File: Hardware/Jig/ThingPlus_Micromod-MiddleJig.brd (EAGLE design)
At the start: 104.1 x 35.6 mm, 67 parts

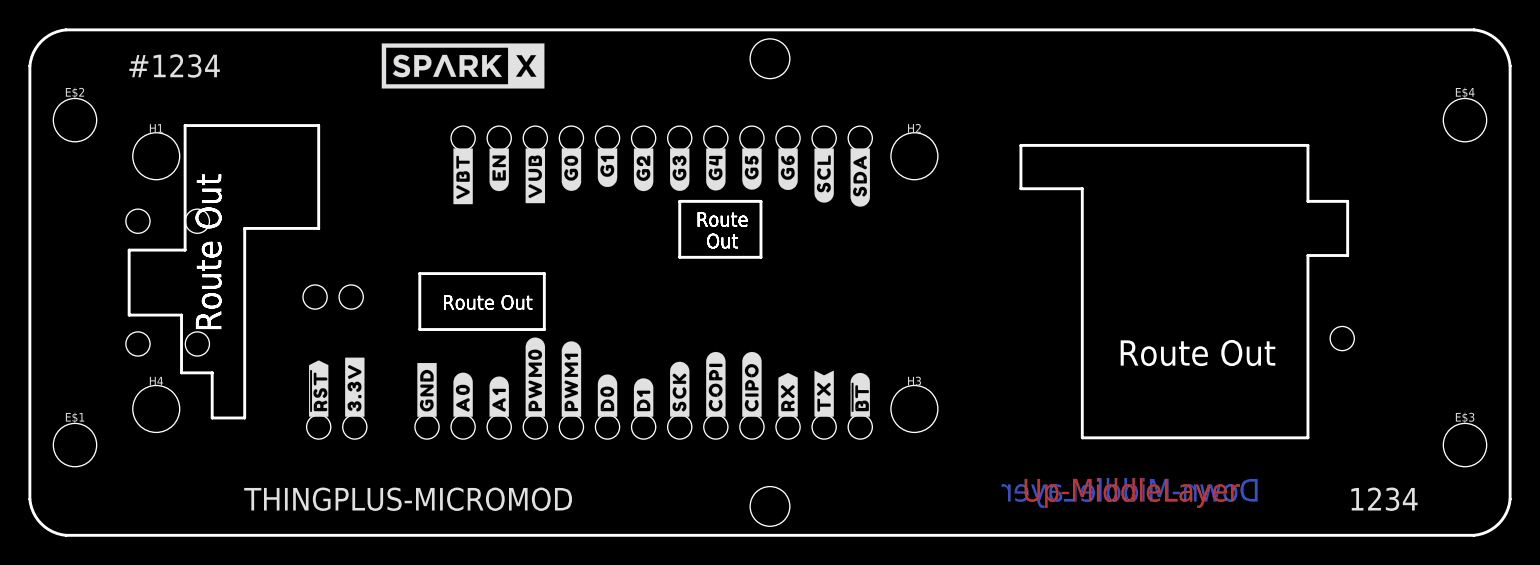
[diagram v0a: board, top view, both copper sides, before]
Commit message: Added jig number, SKU and board names to test jig.
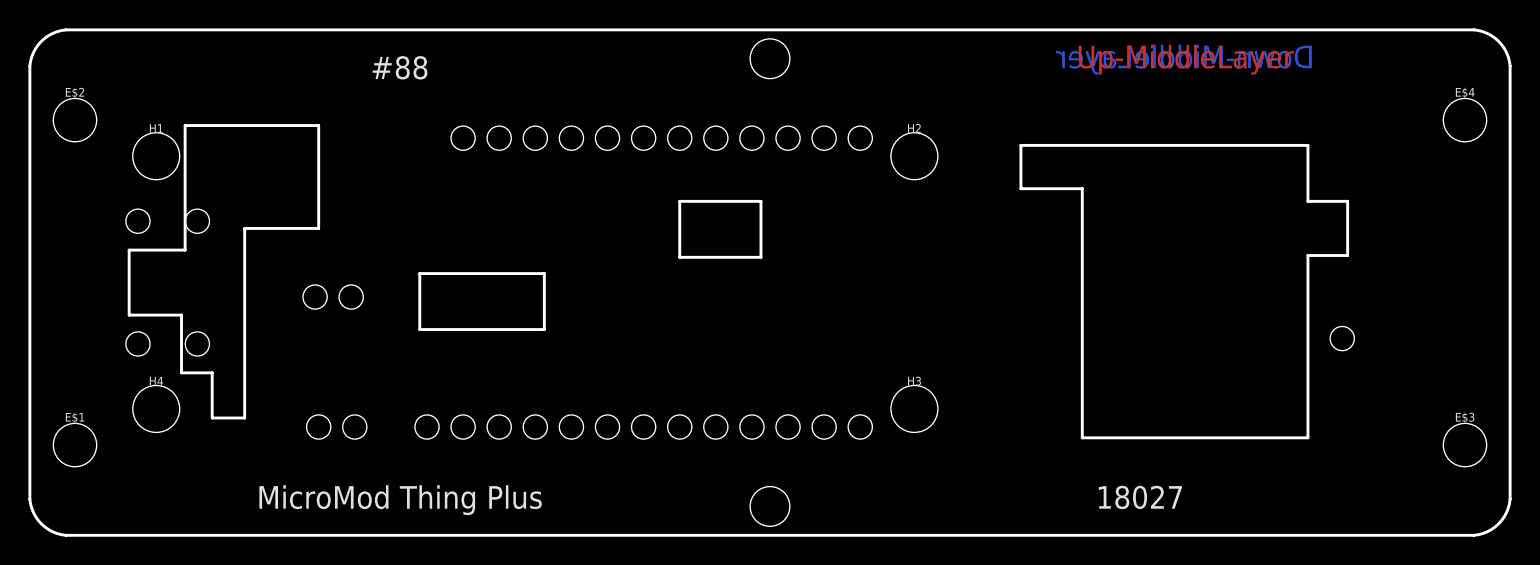
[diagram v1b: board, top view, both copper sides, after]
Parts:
- removed U$1, U$2: SPARKX-LOGO5, SparkX:SPARKX-LARGE
- removed U$10, U$48: (no value), output:#D0#5
- removed U$11, U$49: (no value), output:#PWM0#5
- removed U$12, U$50: (no value), output:#PWM1#5
- removed U$13, U$51: (no value), output:#A1#5
- removed U$14, U$52: (no value), output:#A0#5
- removed U$15, U$53: (no value), output:#GND#4
- removed U$16, U$54: (no value), output:#3#3V#1
- removed U$17, U$55: (no value), output:##RST##0
- removed U$22, U$57: (no value), output:#VBT#16
- removed U$23, U$58: (no value), output:#EN#15
- removed U$24, U$59: (no value), output:#G0#14
- removed U$25, U$60: (no value), output:#G1#14
- removed U$26, U$61: (no value), output:#G2#14
- removed U$27, U$62: (no value), output:#G3#14
- removed U$28, U$63: (no value), output:#G4#14
- removed U$29, U$64: (no value), output:#G5#14
- removed U$3: (no value), output:##BT##11
- removed U$30, U$65: (no value), output:#G6#14
- removed U$31: (no value), output:#SCL#13
- removed U$32, U$67: (no value), output:#SDA#12
- removed U$35, U$68: (no value), output:#VUB#15
- removed U$4, U$42: (no value), output:#TX#9
- removed U$43, U$5: (no value), output:#RX#8
- removed U$44, U$6: (no value), output:#CIPO#7
- removed U$45, U$7: (no value), output:#COPI#6
- removed U$46, U$8: (no value), output:#SCK#5
- removed U$47, U$9: (no value), output:#D1#5
- removed U$56: (no value), output:##BOOT##10
- removed U$71: (no value), output:#SCL#G7#14
- moved FRAME1 4.58 mm to (21.8, 31.5)
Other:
- board text added: "#88"
- board text added: "18027"
- board text added: "MicroMod Thing Plus"
- board text removed: "#1234"
- board text removed: "1234"
- board text removed: "Route Out"
- board text removed: "THINGPLUS-MICROMOD"

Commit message: Added milling polygons to bottom and middle jig boards; created Gerber files.
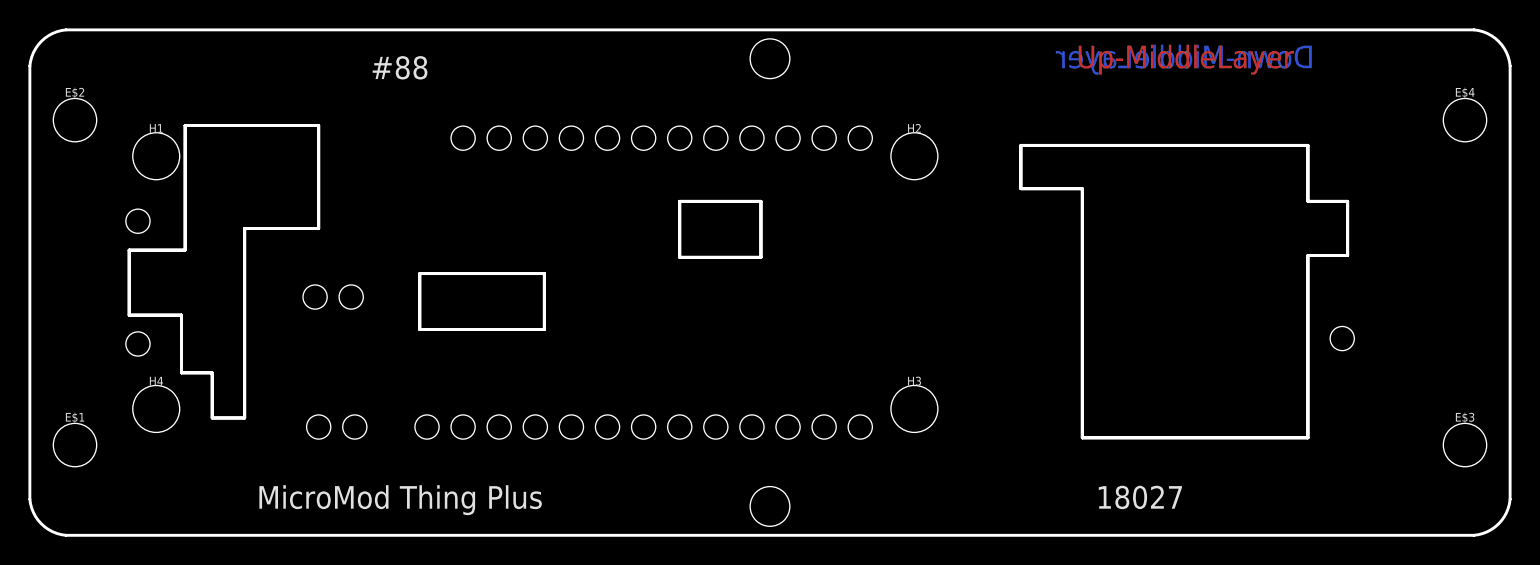
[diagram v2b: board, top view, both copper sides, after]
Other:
- outline, holes or cut-outs redrawn
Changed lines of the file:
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@@
 <setting verticaltext="up"/>
 </settings>
-<grid distance="0.05" unitdist="inch" unit="inch" style="lines" multiple="1" display="yes" altdistance="0.005" altunitdist="inch" altunit="inch"/>
+<grid distance="5" unitdist="mil" unit="mil" style="lines" multiple="1" display="yes" altdistance="1" altunitdist="mil" altunit="mil"/>
 <layers>
 <layer number="1" name="Top" color="4" fill="1" visible="yes" active="yes"/>
@@
 <layer number="44" name="Drills" color="7" fill="1" visible="no" active="yes"/>
 <layer number="45" name="Holes" color="7" fill="1" visible="yes" active="yes"/>
-<layer number="46" name="Milling" color="3" fill="1" visible="no" active="yes"/>
+<layer number="46" name="Milling" color="3" fill="1" visible="yes" active="yes"/>
 <layer number="47" name="Measures" color="7" fill="1" visible="no" active="yes"/>
 <layer number="48" name="Document" color="7" fill="1" visible="no" active="yes"/>
@@
 <hole x="26.67" y="21.59" drill="1.700021875"/>
 <hole x="24.13" y="21.59" drill="1.700021875"/>
-<hole x="5.434990625" y="15.748" drill="1.700021875"/>
-<hole x="5.434990625" y="7.112" drill="1.700021875"/>
 <hole x="1.2549875" y="15.748" drill="1.700021875"/>
 <hole x="1.2549875" y="7.112" drill="1.700021875"/>
@@
 <wire x1="86.36" y1="13.335" x2="86.36" y2="17.145" width="0.2032" layer="20"/>
 <text x="48.26" y="31.496" size="1.778" layer="51" font="vector" ratio="15">Ricardo R.</text>
+<polygon width="0.2032" layer="46">
+<vertex x="0.635" y="13.716"/>
+<vertex x="0.635" y="9.144"/>
+<vertex x="4.318" y="9.144"/>
+<vertex x="4.318" y="5.08"/>
+<vertex x="6.477" y="5.08"/>
+<vertex x="6.477" y="1.905"/>
+<vertex x="8.763" y="1.905"/>
+<vertex x="8.763" y="15.113"/>
+<vertex x="8.763" y="15.24"/>
+<vertex x="13.97" y="15.24"/>
+<vertex x="13.97" y="22.479"/>
+<vertex x="4.572" y="22.479"/>
+<vertex x="4.572" y="13.716"/>
+</polygon>
+<polygon width="0.2032" layer="46">
+<vertex x="21.082" y="12.065"/>
+<vertex x="29.845" y="12.065"/>
+<vertex x="29.845" y="8.128"/>
+<vertex x="21.082" y="8.128"/>
+</polygon>
+<polygon width="0.2032" layer="46">
+<vertex x="39.37" y="17.145"/>
+<vertex x="45.085" y="17.145"/>
+<vertex x="45.085" y="13.208"/>
+<vertex x="39.37" y="13.208"/>
+</polygon>
+<polygon width="0.2032" layer="46">
+<vertex x="63.373" y="21.082"/>
+<vertex x="63.373" y="18.034"/>
+<vertex x="67.691" y="18.034"/>
+<vertex x="67.691" y="0.508"/>
+<vertex x="83.566" y="0.508"/>
+<vertex x="83.566" y="13.335"/>
+<vertex x="86.36" y="13.335"/>
+<vertex x="86.36" y="17.145"/>
+<vertex x="83.566" y="17.145"/>
+<vertex x="83.566" y="21.082"/>
+</polygon>
 </plain>
 <attributes>

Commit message: Updated board and middle jig
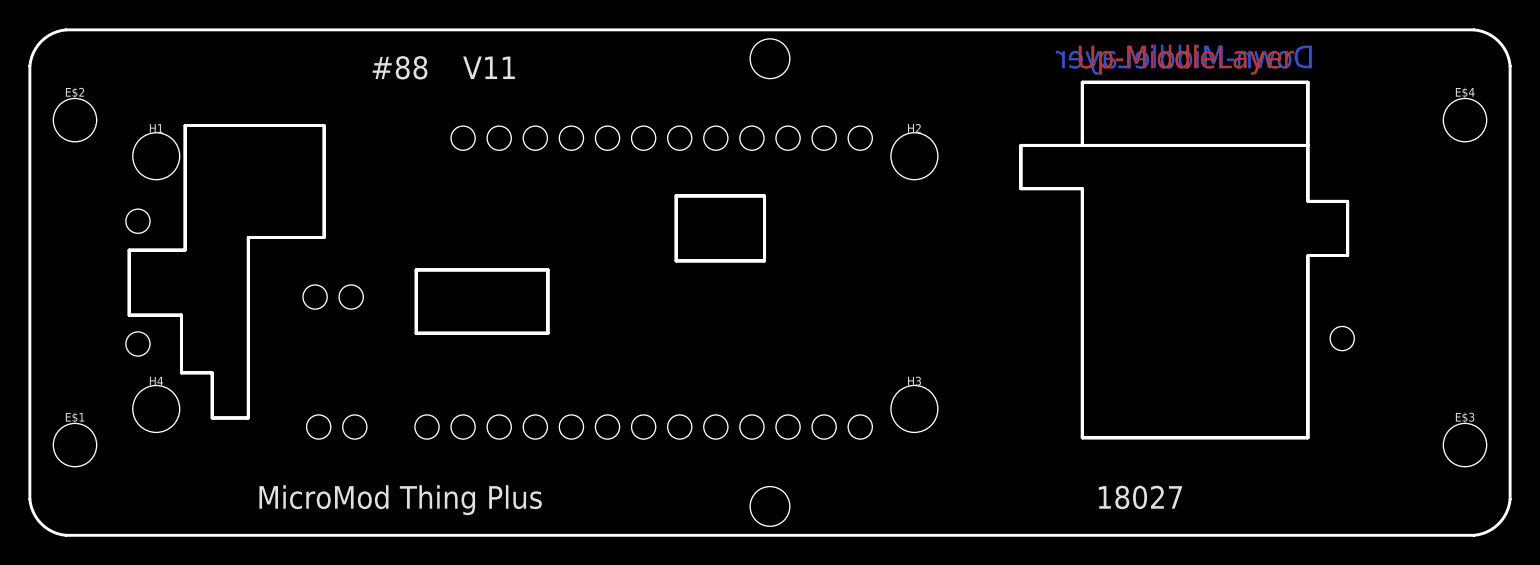
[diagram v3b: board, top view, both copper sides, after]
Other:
- outline, holes or cut-outs redrawn
- board text added: "V11"
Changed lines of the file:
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@@
 <drawing>
 <settings>
-<setting alwaysvectorfont="yes"/>
+<setting alwaysvectorfont="no"/>
 <setting verticaltext="up"/>
 </settings>
-<grid distance="5" unitdist="mil" unit="mil" style="lines" multiple="1" display="yes" altdistance="1" altunitdist="mil" altunit="mil"/>
+<grid distance="0.05" unitdist="inch" unit="inch" style="lines" multiple="1" display="yes" altdistance="0.005" altunitdist="inch" altunit="inch"/>
 <layers>
 <layer number="1" name="Top" color="4" fill="1" visible="yes" active="yes"/>
@@
 <layer number="44" name="Drills" color="7" fill="1" visible="no" active="yes"/>
 <layer number="45" name="Holes" color="7" fill="1" visible="yes" active="yes"/>
-<layer number="46" name="Milling" color="3" fill="1" visible="yes" active="yes"/>
+<layer number="46" name="Milling" color="3" fill="1" visible="no" active="yes"/>
 <layer number="47" name="Measures" color="7" fill="1" visible="no" active="yes"/>
 <layer number="48" name="Document" color="7" fill="1" visible="no" active="yes"/>
@@
 <hole x="1.2549875" y="15.748" drill="1.700021875"/>
 <hole x="1.2549875" y="7.112" drill="1.700021875"/>
-<wire x1="6.477" y1="1.905" x2="8.763" y2="1.905" width="0.2032" layer="20"/>
+<wire x1="6.477" y1="1.905" x2="9.017" y2="1.905" width="0.2032" layer="20"/>
 <wire x1="6.477" y1="5.08" x2="6.477" y2="1.905" width="0.2032" layer="20"/>
-<wire x1="21.082" y1="12.065" x2="29.845" y2="12.065" width="0.2032" layer="20"/>
-<wire x1="29.845" y1="12.065" x2="29.845" y2="8.128" width="0.2032" layer="20"/>
-<wire x1="29.845" y1="8.128" x2="21.082" y2="8.128" width="0.2032" layer="20"/>
-<wire x1="21.082" y1="8.128" x2="21.082" y2="12.065" width="0.2032" layer="20"/>
-<wire x1="39.37" y1="17.145" x2="45.085" y2="17.145" width="0.2032" layer="20"/>
-<wire x1="45.085" y1="17.145" x2="45.085" y2="13.208" width="0.2032" layer="20"/>
-<wire x1="45.085" y1="13.208" x2="39.37" y2="13.208" width="0.2032" layer="20"/>
-<wire x1="39.37" y1="13.208" x2="39.37" y2="17.145" width="0.2032" layer="20"/>
-<wire x1="63.373" y1="21.082" x2="83.566" y2="21.082" width="0.2032" layer="20"/>
-<wire x1="83.566" y1="21.082" x2="83.566" y2="17.145" width="0.2032" layer="20"/>
+<wire x1="20.828" y1="12.319" x2="30.099" y2="12.319" width="0.2032" layer="20"/>
+<wire x1="30.099" y1="12.319" x2="30.099" y2="7.874" width="0.2032" layer="20"/>
+<wire x1="30.099" y1="7.874" x2="20.828" y2="7.874" width="0.2032" layer="20"/>
+<wire x1="20.828" y1="7.874" x2="20.828" y2="12.319" width="0.2032" layer="20"/>
+<wire x1="39.116" y1="17.526" x2="45.339" y2="17.526" width="0.2032" layer="20"/>
+<wire x1="45.339" y1="17.526" x2="45.339" y2="12.954" width="0.2032" layer="20"/>
+<wire x1="45.339" y1="12.954" x2="39.116" y2="12.954" width="0.2032" layer="20"/>
+<wire x1="39.116" y1="12.954" x2="39.116" y2="17.526" width="0.2032" layer="20"/>
 <wire x1="83.566" y1="17.145" x2="86.36" y2="17.145" width="0.2032" layer="20"/>
 <wire x1="83.566" y1="13.335" x2="83.566" y2="0.508" width="0.2032" layer="20"/>
@@
 <wire x1="0.635" y1="13.716" x2="4.572" y2="13.716" width="0.2032" layer="20"/>
 <wire x1="4.572" y1="13.716" x2="4.572" y2="22.479" width="0.2032" layer="20"/>
-<wire x1="4.572" y1="22.479" x2="13.97" y2="22.479" width="0.2032" layer="20"/>
-<wire x1="13.97" y1="22.479" x2="13.97" y2="15.24" width="0.2032" layer="20"/>
-<wire x1="13.97" y1="15.24" x2="8.763" y2="15.24" width="0.2032" layer="20"/>
-<wire x1="8.763" y1="15.24" x2="8.763" y2="1.905" width="0.2032" layer="20"/>
+<wire x1="4.572" y1="22.479" x2="14.351" y2="22.479" width="0.2032" layer="20"/>
+<wire x1="14.351" y1="22.479" x2="14.351" y2="14.605" width="0.2032" layer="20"/>
+<wire x1="14.351" y1="14.605" x2="9.017" y2="14.605" width="0.2032" layer="20"/>
+<wire x1="9.017" y1="14.605" x2="9.017" y2="1.905" width="0.2032" layer="20"/>
 <wire x1="0.635" y1="13.716" x2="0.635" y2="9.144" width="0.2032" layer="20"/>
 <wire x1="0.635" y1="9.144" x2="4.318" y2="9.144" width="0.2032" layer="20"/>
@@
 <vertex x="6.477" y="5.08"/>
 <vertex x="6.477" y="1.905"/>
-<vertex x="8.763" y="1.905"/>
-<vertex x="8.763" y="15.113"/>
-<vertex x="8.763" y="15.24"/>
-<vertex x="13.97" y="15.24"/>
-<vertex x="13.97" y="22.479"/>
+<vertex x="9.017" y="1.905"/>
+<vertex x="9.017" y="14.605"/>
+<vertex x="14.351" y="14.605"/>
+<vertex x="14.351" y="22.479"/>
 <vertex x="4.572" y="22.479"/>
 <vertex x="4.572" y="13.716"/>
 </polygon>
 <polygon width="0.2032" layer="46">
-<vertex x="21.082" y="12.065"/>
-<vertex x="29.845" y="12.065"/>
-<vertex x="29.845" y="8.128"/>
-<vertex x="21.082" y="8.128"/>
-</polygon>
-<polygon width="0.2032" layer="46">
-<vertex x="39.37" y="17.145"/>
-<vertex x="45.085" y="17.145"/>
-<vertex x="45.085" y="13.208"/>
-<vertex x="39.37" y="13.208"/>
+<vertex x="20.828" y="12.319"/>
+<vertex x="30.099" y="12.319"/>
+<vertex x="30.099" y="7.874"/>
+<vertex x="20.828" y="7.874"/>
+</polygon>
+<polygon width="0.2032" layer="46">
+<vertex x="39.116" y="17.526"/>
+<vertex x="45.339" y="17.526"/>
+<vertex x="45.339" y="12.954"/>
+<vertex x="39.116" y="12.954"/>
 </polygon>
 <polygon width="0.2032" layer="46">
@@
 <vertex x="83.566" y="21.082"/>
 </polygon>
+<wire x1="63.373" y1="21.082" x2="67.691" y2="21.082" width="0.2032" layer="20"/>
+<wire x1="67.691" y1="21.082" x2="67.691" y2="25.527" width="0.2032" layer="20"/>
+<wire x1="67.691" y1="25.527" x2="83.566" y2="25.527" width="0.2032" layer="20"/>
+<wire x1="83.566" y1="25.527" x2="83.566" y2="17.145" width="0.2032" layer="20"/>
+<polygon width="0.2032" layer="46">
+<vertex x="67.691" y="21.082"/>
+<vertex x="67.691" y="25.527"/>
+<vertex x="83.566" y="25.527"/>
+<vertex x="83.566" y="21.082"/>
+</polygon>
+<text x="26.035" y="26.543" size="1.5875" layer="21" font="vector" ratio="15" align="center">V11</text>
+<dimension x1="-6.35" y1="-8.89" x2="97.79" y2="-8.89" x3="45.72" y3="-15.24" textsize="1.778" textratio="15" layer="1"/>
 </plain>
 <attributes>
